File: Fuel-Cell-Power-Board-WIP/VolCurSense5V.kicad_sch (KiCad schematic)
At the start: 6 parts, among them U7 ACS770xCB-050B-PFF, U7 TSV912IDT

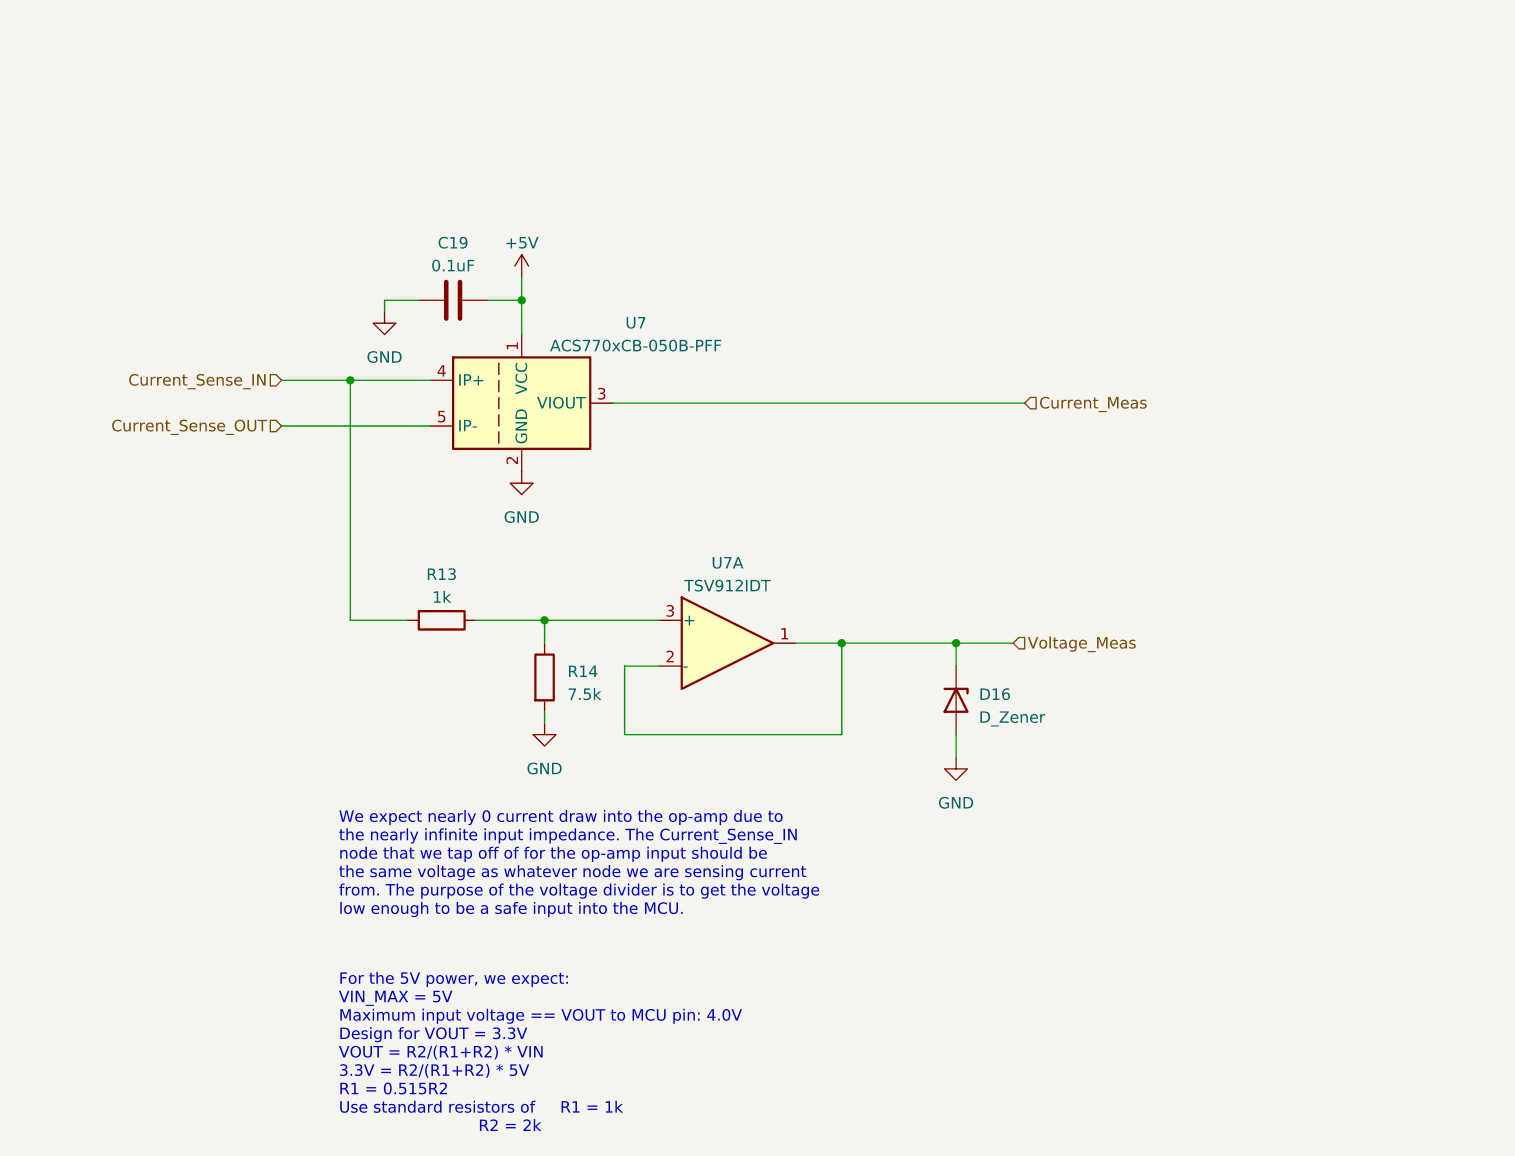
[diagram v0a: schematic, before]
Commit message: Major changes: removed 12V reg, added battery power for 5V/12V, revised current sensing modules to have a smaller upper limit, added voltage divider + op-amp for more measurements.
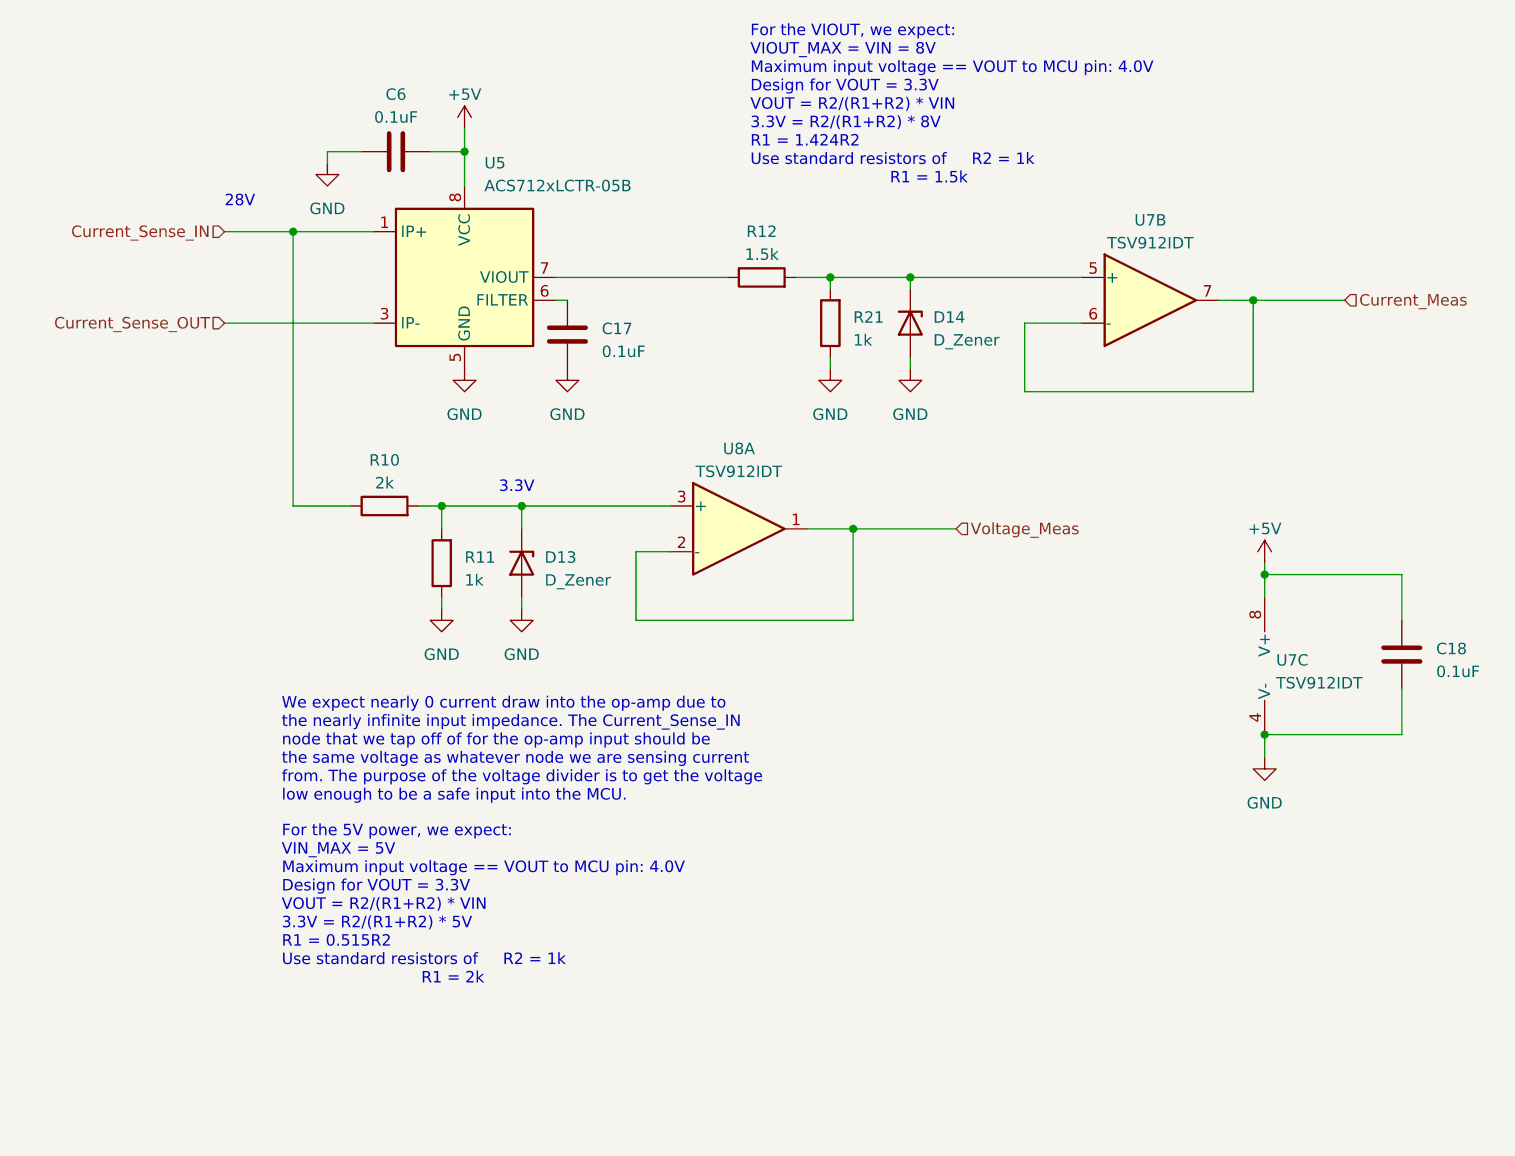
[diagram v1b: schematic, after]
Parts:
- removed C19: 0.1uF, symbol Device:C
- removed D16: D_Zener, symbol Device:D_Zener
- removed R13: 1k, symbol Device:R
- removed R14: 7.5k, symbol Device:R
- removed U7: TSV912IDT, symbol Amplifier_Operational:TSV912IDT
- removed U7: ACS770xCB-050B-PFF, Sensor_Current:Allegro_CB_PFF, symbol Sensor_Current:ACS770xCB-050B-PFF
- added C17, C18, C6: 0.1uF, symbol Device:C
- added D13, D14: D_Zener, symbol Device:D_Zener
- added R10: 2k, symbol Device:R
- added R11, R21: 1k, symbol Device:R
- added R12: 1.5k, symbol Device:R
- added U5: ACS712xLCTR-05B, Package_SO:SOIC-8_3.9x4.9mm_P1.27mm, symbol Sensor_Current:ACS712xLCTR-05B
- added U7, U8: TSV912IDT, symbol Amplifier_Operational:TSV912IDT
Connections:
- net +5V: now also C18.2, C6.2, U5.8 (VCC), U7.8 (V+)
- net Current_Meas: now also U7.6 (-), U7.7
- net Current_Sense_IN: now also R10.1, U5.1 (IP+), U5.2 (IP+)
- net Current_Sense_OUT: now also U5.3 (IP-), U5.4 (IP-)
- net GND: now also C17.1, C18.1, C6.1, D13.2 (A), D14.2 (A), R11.1, R21.1, U5.5 (GND), U7.4 (V-)
- net Voltage_Meas: now also U8.1, U8.2 (-)
- new net: R12.1, U5.7 (VIOUT)
- new net: D14.1 (K), R12.2, R21.2, U7.5 (+)
- new net: D13.1 (K), R10.2, R11.2, U8.3 (+)
- new net: C17.2, U5.6 (FILTER)
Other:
- note added: "28V"
- note added: "3.3V"
- note added: "For the 5V power, we expect: VIN_MAX = 5V Maximum input voltage == VOUT to MCU pin: 4.0V Design for VOUT = 3.3V VOUT = R2/(R1+R2) * VIN 3.3V = R2/(R1+R2) * 5V R1 = 0.515R2 Use standard resistors of R2 = 1k R1 = 2k"
- note added: "For the VIOUT, we expect: VIOUT_MAX = VIN = 8V Maximum input voltage == VOUT to MCU pin: 4.0V Design for VOUT = 3.3V VOUT = R2/(R1+R2) * VIN 3.3V = R2/(R1+R2) * 8V R1 = 1.424R2 Use standard resistors of R2 = 1k R1 = 1.5k"
- note removed: "For the 5V power, we expect: VIN_MAX = 5V Maximum input voltage == VOUT to MCU pin: 4.0V Design for VOUT = 3.3V VOUT = R2/(R1+R2) * VIN 3.3V = R2/(R1+R2) * 5V R1 = 0.515R2 Use standard resistors of R1 = 1k R2 = 2k"

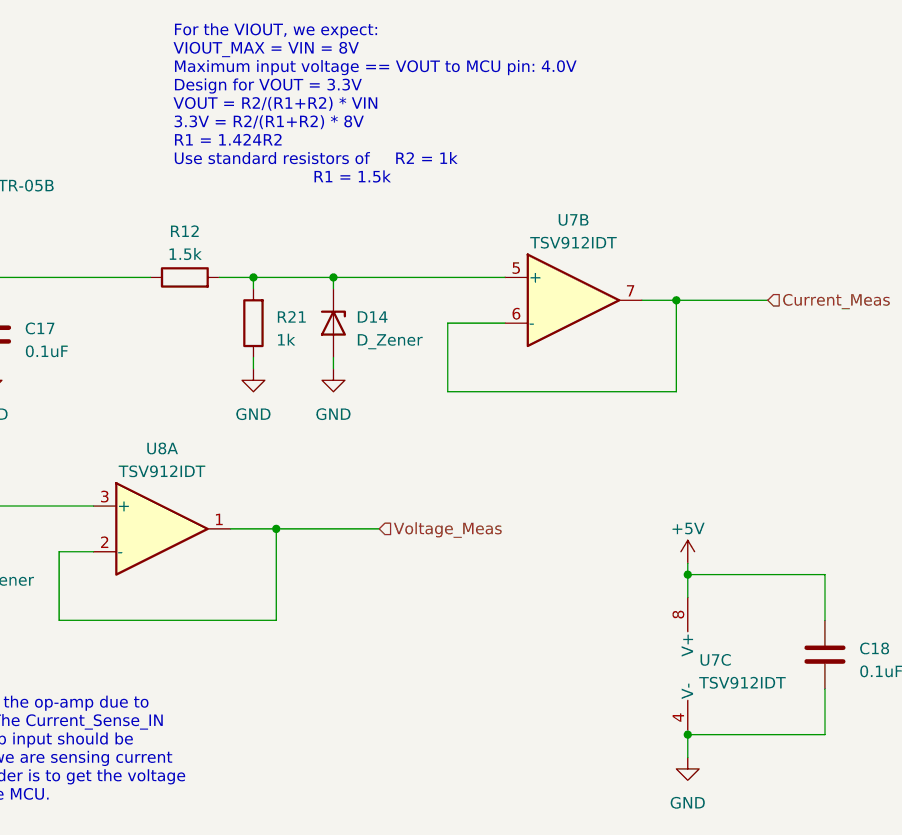
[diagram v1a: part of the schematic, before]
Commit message: made changes to Power flow stuff
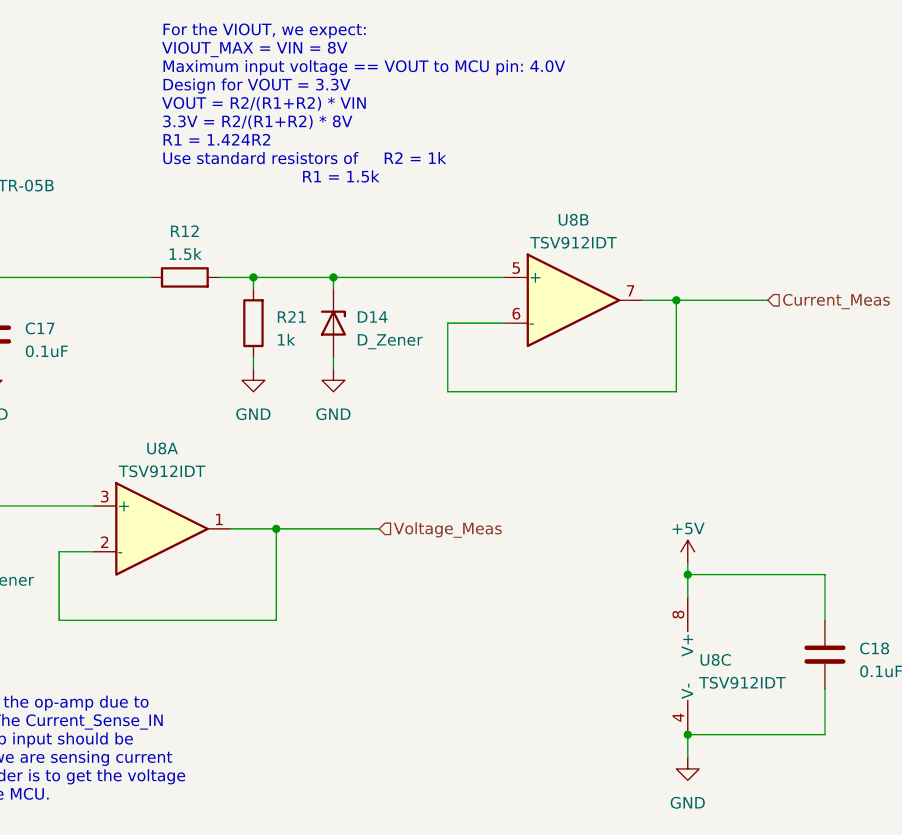
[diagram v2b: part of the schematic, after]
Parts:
- renumbered U7 to U8
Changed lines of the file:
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@@
   )
   (text "For the VIOUT, we expect:\nVIOUT_MAX = VIN = 8V\nMaximum input voltage == VOUT to MCU pin: 4.0V\nDesign for VOUT = 3.3V\nVOUT = R2/(R1+R2) * VIN\n3.3V = R2/(R1+R2) * 8V\nR1 = 1.424R2\nUse standard resistors of 	R2 = 1k\n							R1 = 1.5k"
-    (at 93.98 43.18 0)
+    (at 92.71 43.18 0)
     (effects (font (size 1.27 1.27)) (justify left bottom))
   )
@@
   (symbol (lib_id "Amplifier_Operational:TSV912IDT") (at 153.67 96.52 0) (unit 3)
     (in_bom yes) (on_board yes) (dnp no) (fields_autoplaced)
-    (property "Reference" "U7" (at 152.4 95.885 0)
+    (property "Reference" "U8" (at 152.4 95.885 0)
       (effects (font (size 1.27 1.27)) (justify left))
     )
@@
   (symbol (lib_id "Amplifier_Operational:TSV912IDT") (at 138.43 55.88 0) (unit 2)
     (in_bom yes) (on_board yes) (dnp no) (fields_autoplaced)
-    (property "Reference" "U7" (at 138.43 46.99 0)
-      (effects (font (size 1.27 1.27)))
-    )
+    (property "Reference" "U8" (at 138.43 46.99 0)
+      (effects (font (size 1.27 1.27)))
+    )

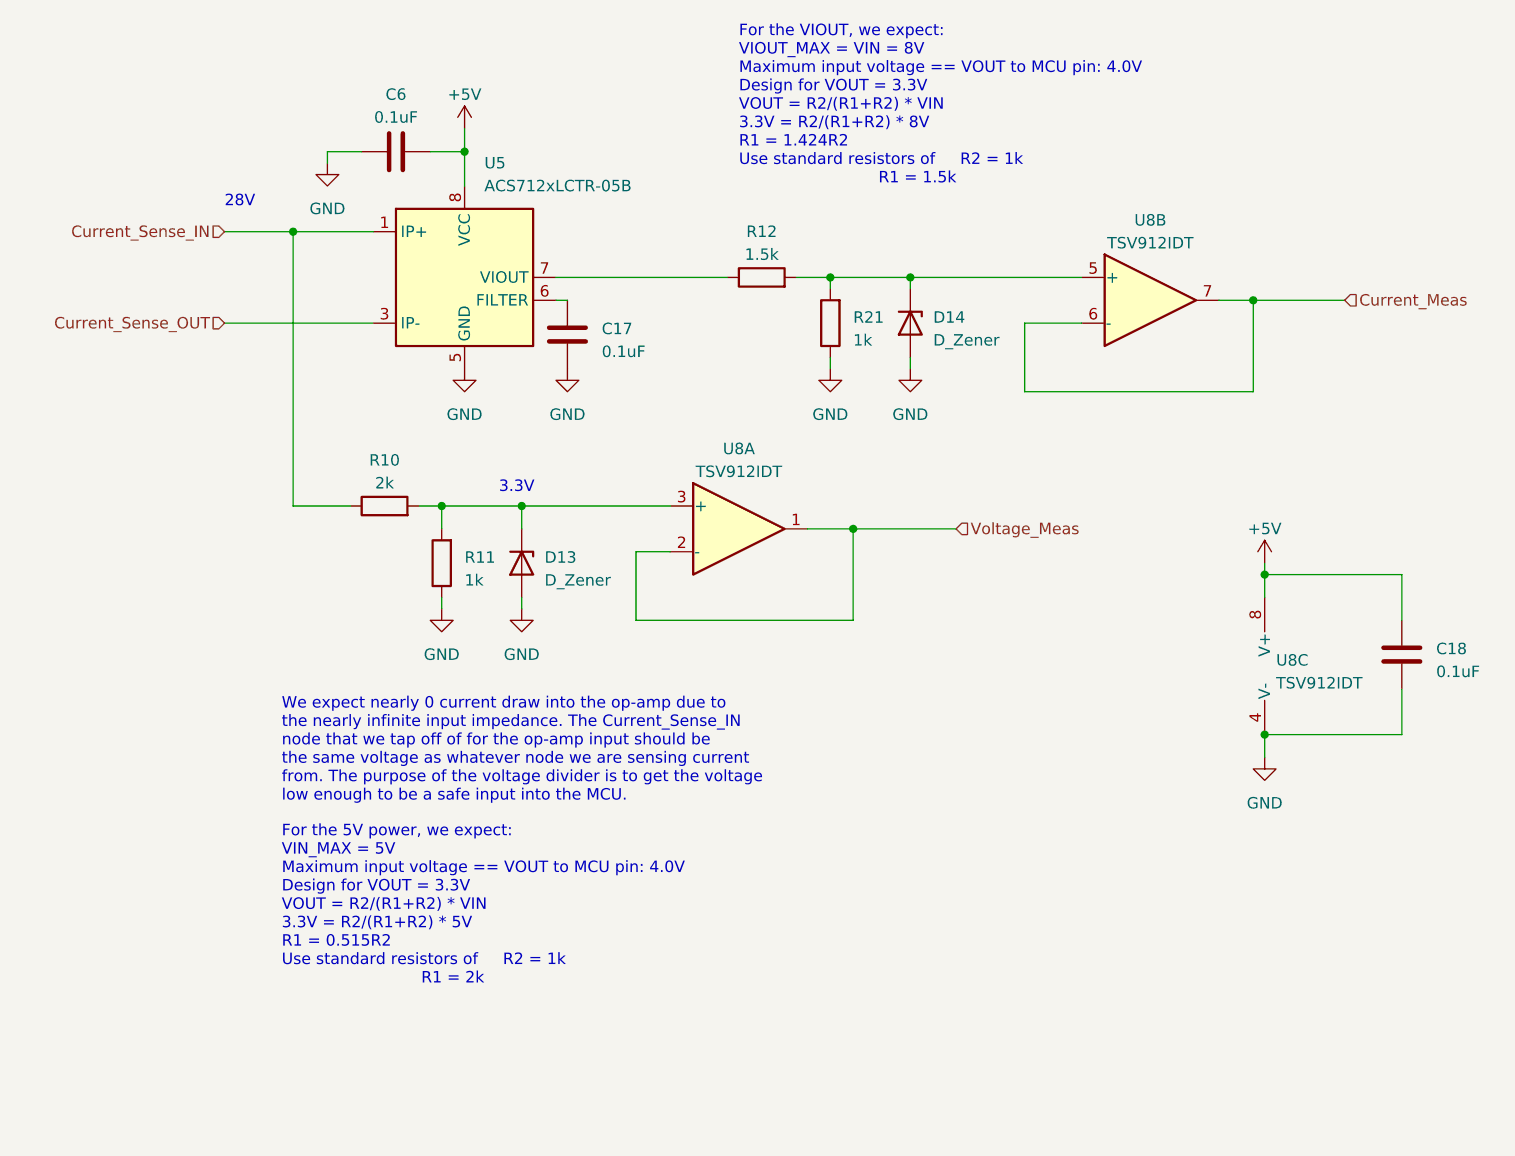
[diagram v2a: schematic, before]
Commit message: Picked most of the parts except for some resistors
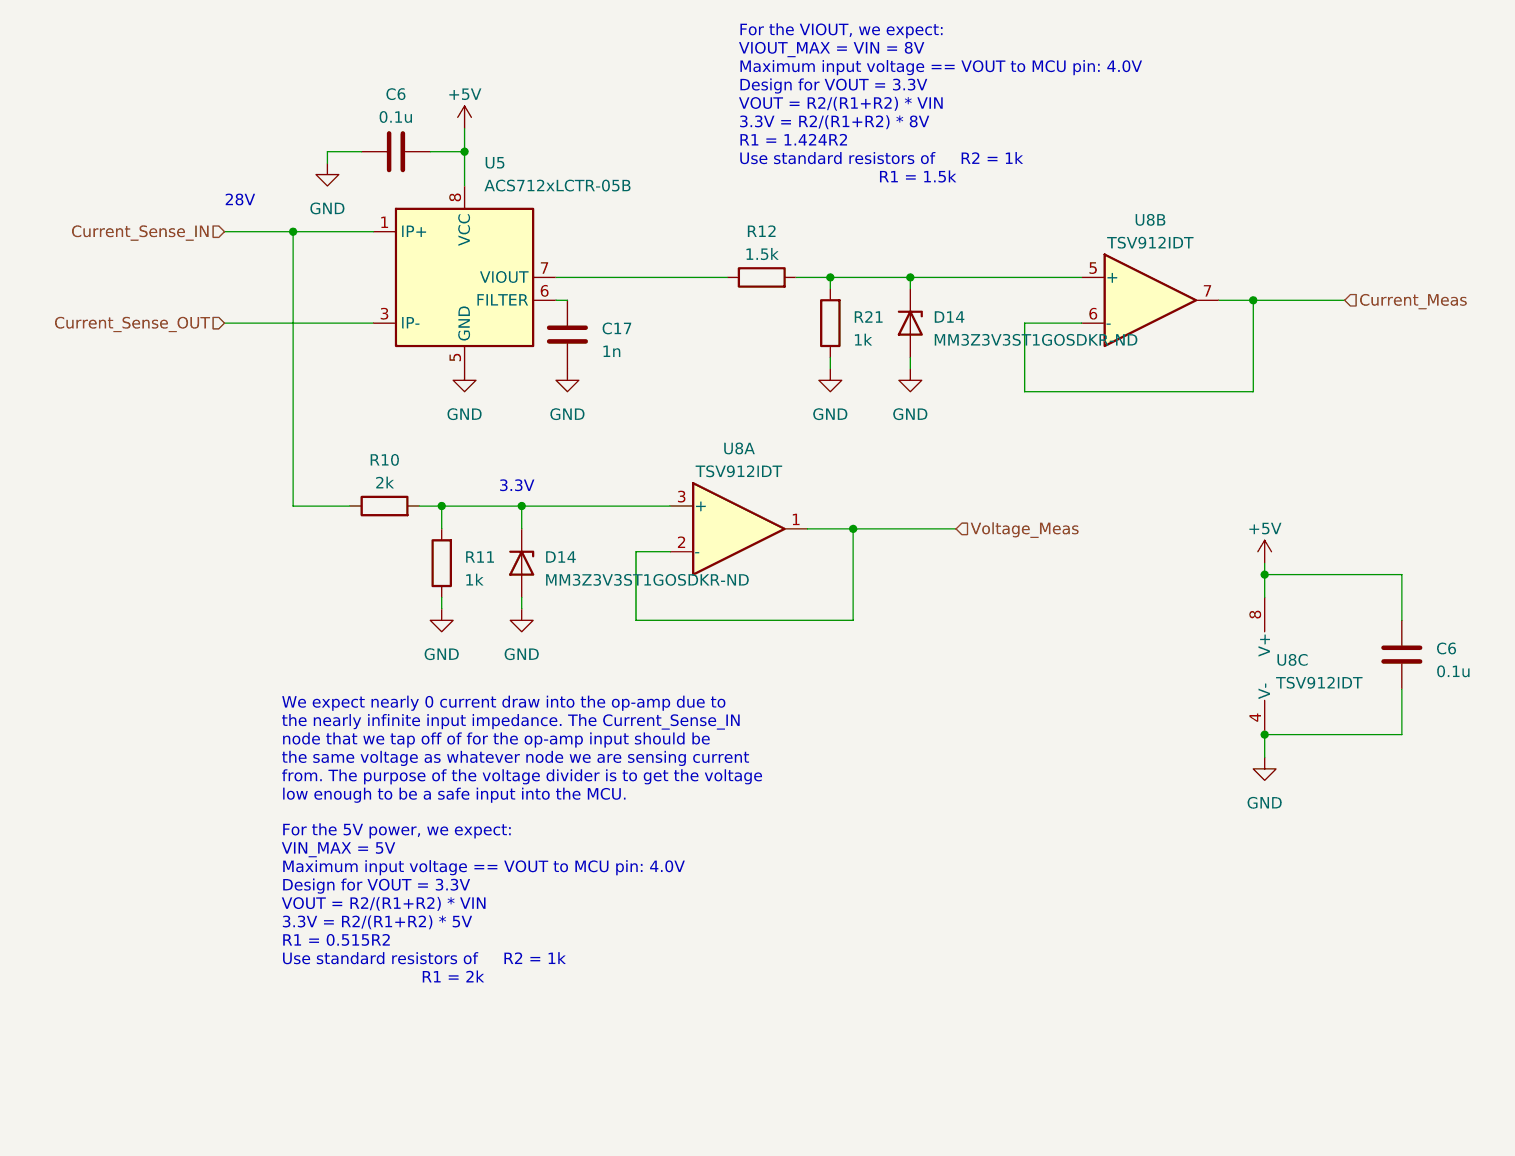
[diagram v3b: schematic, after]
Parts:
- removed C18, C6: 0.1uF, symbol Device:C
- removed D13, D14: D_Zener, symbol Device:D_Zener
- added C6 (x2): 0.1u, Capacitor_SMD:C_0603_1608Metric, symbol Device:C
- added D14 (x2): MM3Z3V3ST1GOSDKR-ND, FPCB_Footprints:SOD-323_1P8X1P35_ONS, symbol Device:D_Zener
- C17: value 0.1uF -> 1n; footprint (none) -> Capacitor_SMD:C_0603_1608Metric; Part (none) -> CC0603JRX7R7BB102
- R10, R11, R12, R21: footprint (none) -> Resistor_SMD:R_0805_2012Metric
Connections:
- net +5V: now also C6.1, C6.2
- net GND: now also C6.1, C6.2, D14.2 (A), D14.2 (A)
- net at R12.2, R21.2, U8.5 (+): now also D14.1 (K)
- net at R10.2, R11.2, U8.3 (+): now also D14.1 (K)
